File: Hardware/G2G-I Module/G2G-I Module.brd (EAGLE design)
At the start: 13.1 x 12.8 mm, 4 parts, among them J1 GROVE-4P-2.0-3470130P1

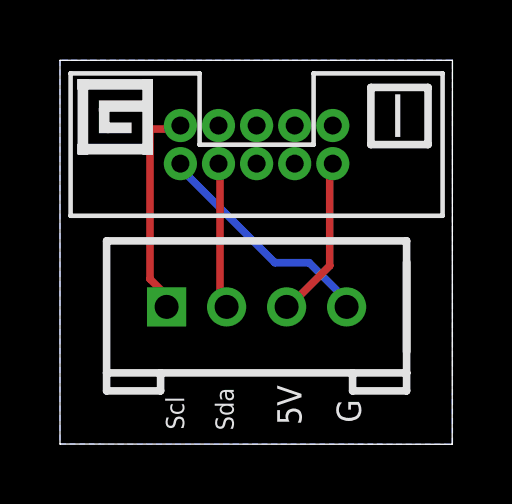
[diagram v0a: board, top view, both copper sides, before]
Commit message: Rotated the G plug 180 degrees.
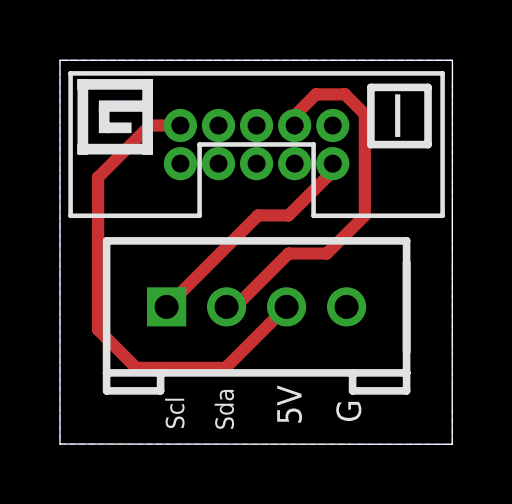
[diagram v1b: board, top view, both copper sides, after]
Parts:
- turned U$1 to 180 degrees
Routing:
- net +5V: track 5.47 -> 16.2 mm
- net GND: track 7.74 -> 0.00 mm
- net SDA: track 4.93 -> 12.5 mm
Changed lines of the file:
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@@
 <element name="J1" library="SoftDust" package="4P-2.0" value="GROVE-4P-2.0-3470130P1" x="6.5532" y="4.572" smashed="yes"/>
 <element name="LOGO1" library="SparkFun-Aesthetics" package="OSHW-LOGO-S" value="OSHW-LOGOS" x="1.8796" y="1.778" rot="MR0"/>
-<element name="U$1" library="SoftDust" package="2X5_1.27MM_FEMALE_PLUG" value="2X5_1.27MM_FEMALE_PLUG" x="6.5532" y="9.9822" rot="MR0"/>
+<element name="U$1" library="SoftDust" package="2X5_1.27MM_FEMALE_PLUG" value="2X5_1.27MM_FEMALE_PLUG" x="6.5532" y="9.9822" rot="MR180"/>
 <element name="FRAME1" library="SparkFun-Aesthetics" package="DUMMY" value="" x="0" y="-1.27">
 <attribute name="VERSION" value="v1.0" x="0" y="-1.27" size="1.778" layer="27" display="off"/>
@@
 <contactref element="U$1" pad="10"/>
 <contactref element="J1" pad="4"/>
-<wire x1="4.191" y1="9.017" x2="4.191" y2="9.2456" width="0.254" layer="16"/>
-<wire x1="7.1628" y1="6.0452" x2="4.191" y2="9.017" width="0.254" layer="16"/>
-<wire x1="8.3058" y1="6.0452" x2="7.1628" y2="6.0452" width="0.254" layer="16"/>
-<wire x1="9.4488" y1="4.9022" x2="8.3058" y2="6.0452" width="0.254" layer="16"/>
-<wire x1="4.191" y1="9.2456" x2="4.0132" y2="9.3472" width="0.254" layer="16"/>
-<wire x1="9.4488" y1="4.9022" x2="9.5532" y2="4.572" width="0.254" layer="16"/>
 <polygon width="0.254" layer="16" isolate="0.4064">
 <vertex x="0" y="0"/>
@@
 <contactref element="J1" pad="3"/>
 <contactref element="U$1" pad="2"/>
-<wire x1="8.9916" y1="5.9436" x2="8.9916" y2="9.2964" width="0.254" layer="1"/>
-<wire x1="7.62" y1="4.572" x2="8.9916" y2="5.9436" width="0.254" layer="1"/>
-<wire x1="8.9916" y1="9.2964" x2="9.0932" y2="9.3472" width="0.1524" layer="1"/>
-<wire x1="7.62" y1="4.572" x2="7.5532" y2="4.572" width="0.1524" layer="1"/>
+<wire x1="7.5532" y1="4.572" x2="5.5212" y2="2.54" width="0.4064" layer="1"/>
+<wire x1="5.5212" y1="2.54" x2="2.54" y2="2.54" width="0.4064" layer="1"/>
+<wire x1="2.54" y1="2.54" x2="1.27" y2="3.81" width="0.4064" layer="1"/>
+<wire x1="1.27" y1="3.81" x2="1.27" y2="8.89" width="0.4064" layer="1"/>
+<wire x1="1.27" y1="8.89" x2="2.9972" y2="10.6172" width="0.4064" layer="1"/>
+<wire x1="2.9972" y1="10.6172" x2="4.0132" y2="10.6172" width="0.4064" layer="1"/>
 </signal>
 <signal name="SDA">
 <contactref element="U$1" pad="8"/>
 <contactref element="J1" pad="2"/>
-<wire x1="5.334" y1="4.7244" x2="5.334" y2="9.2964" width="0.254" layer="1"/>
-<wire x1="5.4864" y1="4.572" x2="5.334" y2="4.7244" width="0.1524" layer="1"/>
-<wire x1="5.334" y1="9.2964" x2="5.2832" y2="9.3472" width="0.1524" layer="1"/>
-<wire x1="5.4864" y1="4.572" x2="5.5532" y2="4.572" width="0.1524" layer="1"/>
+<wire x1="5.5532" y1="4.572" x2="5.842" y2="4.572" width="0.4064" layer="1"/>
+<wire x1="5.842" y1="4.572" x2="7.62" y2="6.35" width="0.4064" layer="1"/>
+<wire x1="7.62" y1="6.35" x2="8.89" y2="6.35" width="0.4064" layer="1"/>
+<wire x1="8.89" y1="6.35" x2="10.16" y2="7.62" width="0.4064" layer="1"/>
+<wire x1="10.16" y1="7.62" x2="10.16" y2="10.9982" width="0.4064" layer="1"/>
+<wire x1="10.16" y1="10.9982" x2="9.4996" y2="11.6586" width="0.4064" layer="1"/>
+<wire x1="9.4996" y1="11.6586" x2="8.5344" y2="11.6586" width="0.4064" layer="1"/>
+<wire x1="8.5344" y1="11.6586" x2="7.8232" y2="10.9474" width="0.4064" layer="1"/>
+<wire x1="7.8232" y1="10.9474" x2="7.8232" y2="10.6172" width="0.4064" layer="1"/>
 </signal>
 <signal name="SCL">
 <contactref element="J1" pad="1"/>
 <contactref element="U$1" pad="9"/>
-<wire x1="3" y1="10.5" x2="4" y2="10.5" width="0.254" layer="1"/>
-<wire x1="3" y1="5.5" x2="3" y2="10.5" width="0.254" layer="1"/>
-<wire x1="3.5" y1="5" x2="3" y2="5.5" width="0.254" layer="1"/>
-<wire x1="4" y1="10.5" x2="4.0132" y2="10.6172" width="0.254" layer="1"/>
-<wire x1="3.5" y1="5" x2="3.5532" y2="4.572" width="0.254" layer="1"/>
+<wire x1="3.5532" y1="4.572" x2="6.6012" y2="7.62" width="0.4064" layer="1"/>
+<wire x1="6.6012" y1="7.62" x2="7.62" y2="7.62" width="0.4064" layer="1"/>
+<wire x1="7.62" y1="7.62" x2="8.89" y2="8.89" width="0.4064" layer="1"/>
+<wire x1="8.89" y1="8.89" x2="8.89" y2="9.144" width="0.4064" layer="1"/>
+<wire x1="8.89" y1="9.144" x2="9.0932" y2="9.3472" width="0.4064" layer="1"/>
 </signal>
 </signals>

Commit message: Replaced all 'G' logos with a new part for the logo.
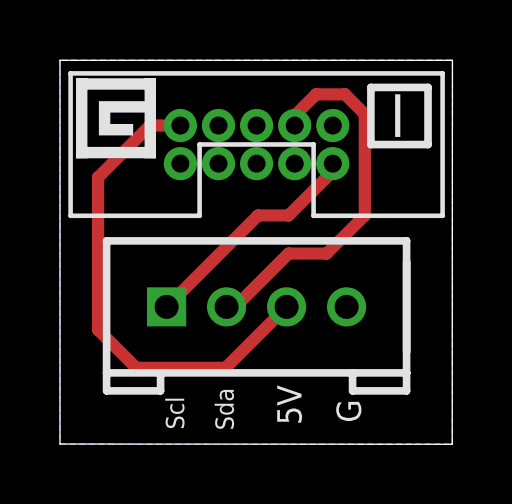
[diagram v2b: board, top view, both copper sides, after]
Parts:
- added U$2: GADGETEER_LOGO_SMALL, SoftDust:GADGETEER_LOGO_SMALL
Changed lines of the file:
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@@
 <text x="10.033" y="0.7112" size="0.8128" layer="21" font="vector" rot="R90">G</text>
 <text x="11.6586" y="6.0198" size="1.016" layer="22" font="vector" rot="MR0">Gadgeteer.in'</text>
-<rectangle x1="0.5842" y1="9.652" x2="3.0988" y2="10.0076" layer="21"/>
-<rectangle x1="0.5842" y1="11.811" x2="3.0988" y2="12.1666" layer="21"/>
-<rectangle x1="1.6637" y1="10.7315" x2="4.1783" y2="11.0871" layer="21" rot="R90"/>
-<rectangle x1="-0.4953" y1="10.7315" x2="2.0193" y2="11.0871" layer="21" rot="R90"/>
-<rectangle x1="1.2954" y1="11.0744" x2="2.7686" y2="11.4554" layer="21"/>
-<rectangle x1="1.2954" y1="10.3632" x2="1.651" y2="11.2014" layer="21"/>
-<rectangle x1="1.7907" y1="10.1219" x2="2.1463" y2="10.9601" layer="21" rot="R90"/>
 </plain>
 <attributes>
@@
 <attribute name="DESIGNER" value="Ian Lee" x="0" y="-1.27" size="1.778" layer="27" display="off"/>
 </element>
+<element name="U$2" library="SoftDust" package="GADGETEER_LOGO_SMALL" value="GADGETEER_LOGO_SMALL" x="0.5334" y="9.525"/>
 </elements>
 <signals>
